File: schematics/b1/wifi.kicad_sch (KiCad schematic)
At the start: 14 parts, among them J1 SERIAL, SW2 RESET, SW3 BOOT, U2 ESP-12F, U9 MCP23017_SP

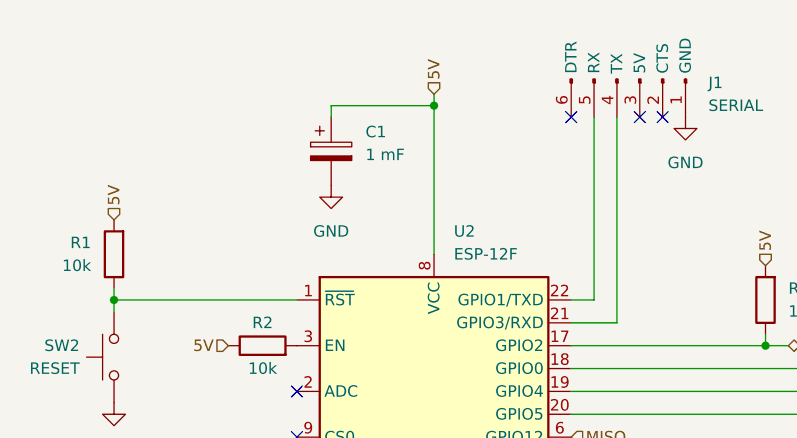
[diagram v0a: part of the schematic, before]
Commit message: Wired LoRa and added a bulk to the status block.
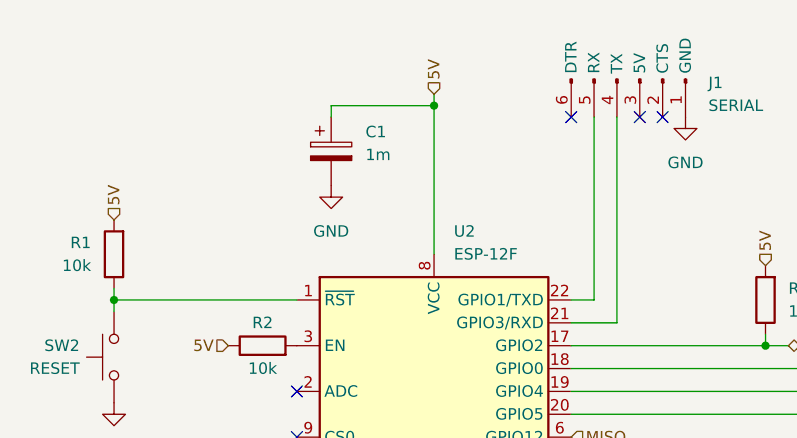
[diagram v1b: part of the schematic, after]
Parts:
- C1: value 1 mF -> 1m
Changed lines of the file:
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@@
       (effects (font (size 1.27 1.27)) (justify left))
     )
-    (property "Value" "1 mF" (at 85.09 62.611 0)
+    (property "Value" "1m" (at 85.09 62.611 0)
       (effects (font (size 1.27 1.27)) (justify left))
     )

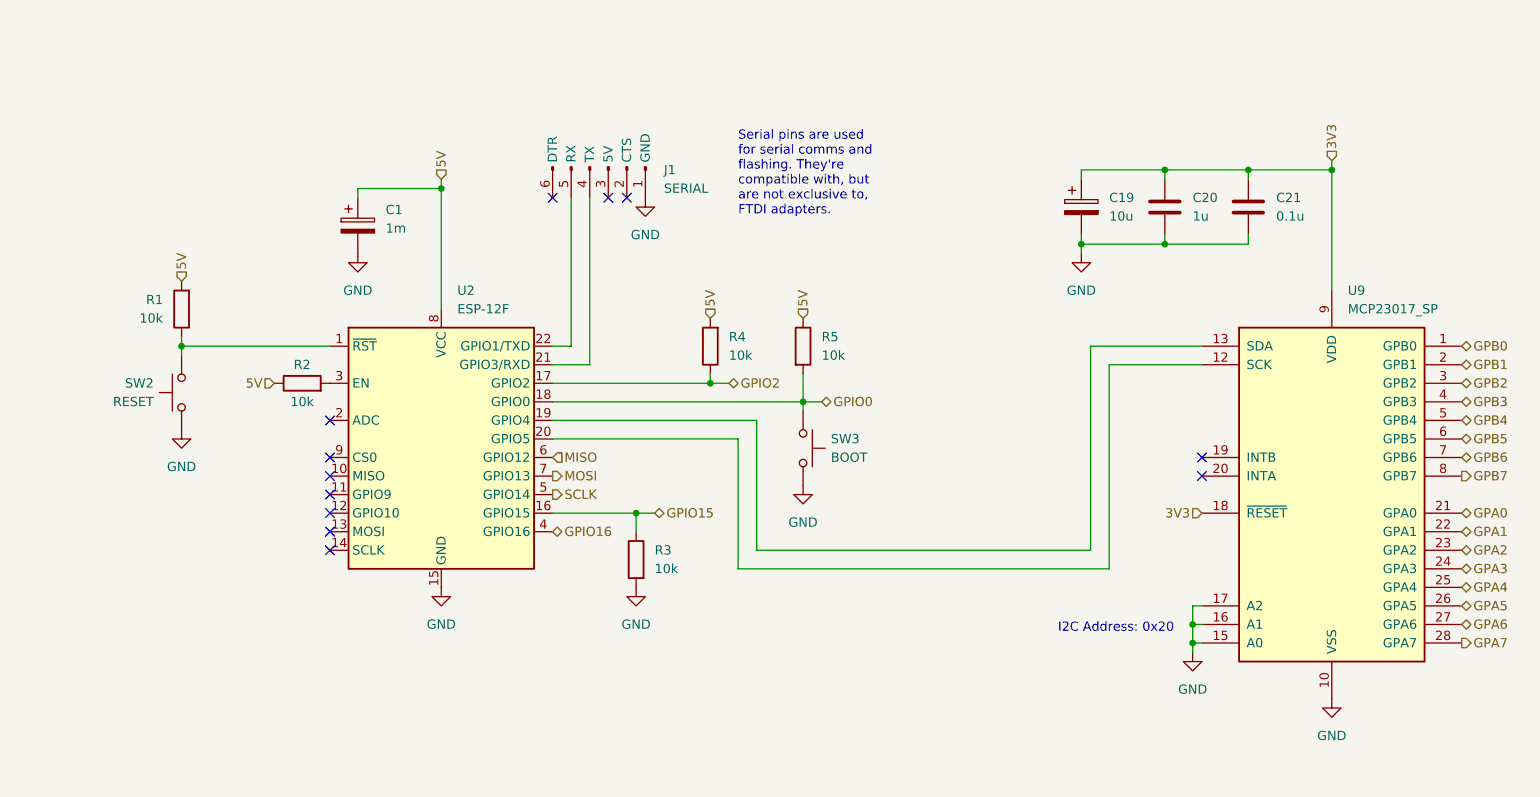
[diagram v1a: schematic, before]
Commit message: Increased capacitance and added some test points.
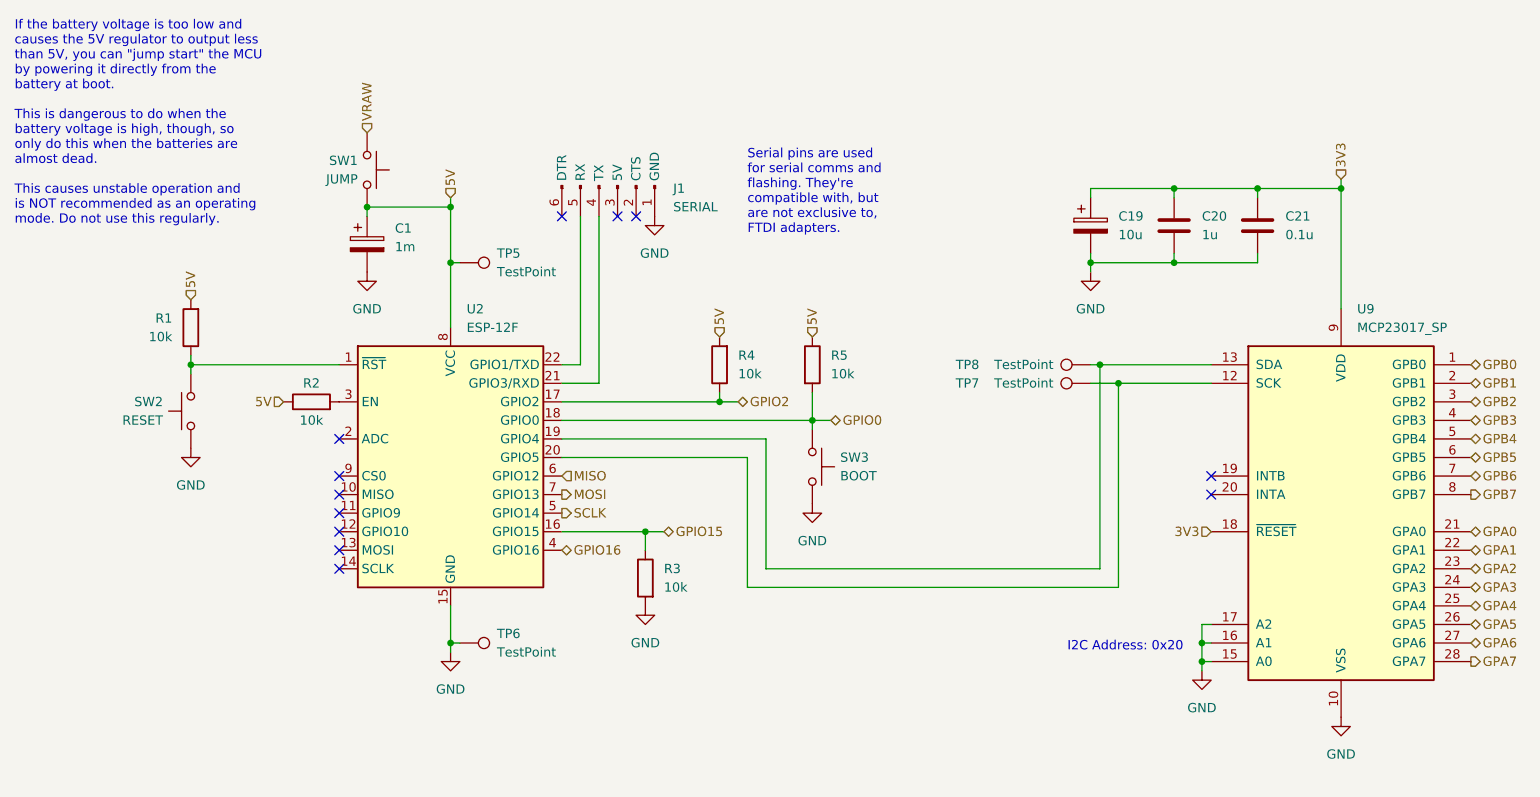
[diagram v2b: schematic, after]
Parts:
- added SW1: JUMP, symbol Switch:SW_Push
- added TP5, TP6, TP7, TP8: TestPoint, symbol Connector:TestPoint
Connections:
- net 5V: now also SW1.1, TP5.1
- net GND: now also TP6.1
- net at U2.19 (GPIO4), U9.13 (SDA): now also TP8.1
- net at U2.20 (GPIO5), U9.12 (SCK): now also TP7.1
- new net VRAW: SW1.2
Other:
- note added: "If the battery voltage is too low and causes the 5V regulator to output less than 5V, you can "jump start" the MCU by powering it directly from the battery at boot. This is dangerous to do when the battery voltage is high, though, so only do this when the batteries are almost dead. This causes unstable operation and is NOT recommended as an operating mode. Do not use this regularly."
- moved on the sheet: C1, C19, C20, C21, J1, R1, R2, R3, R4, R5, SW2, SW3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

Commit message: Added a bunch of test points.
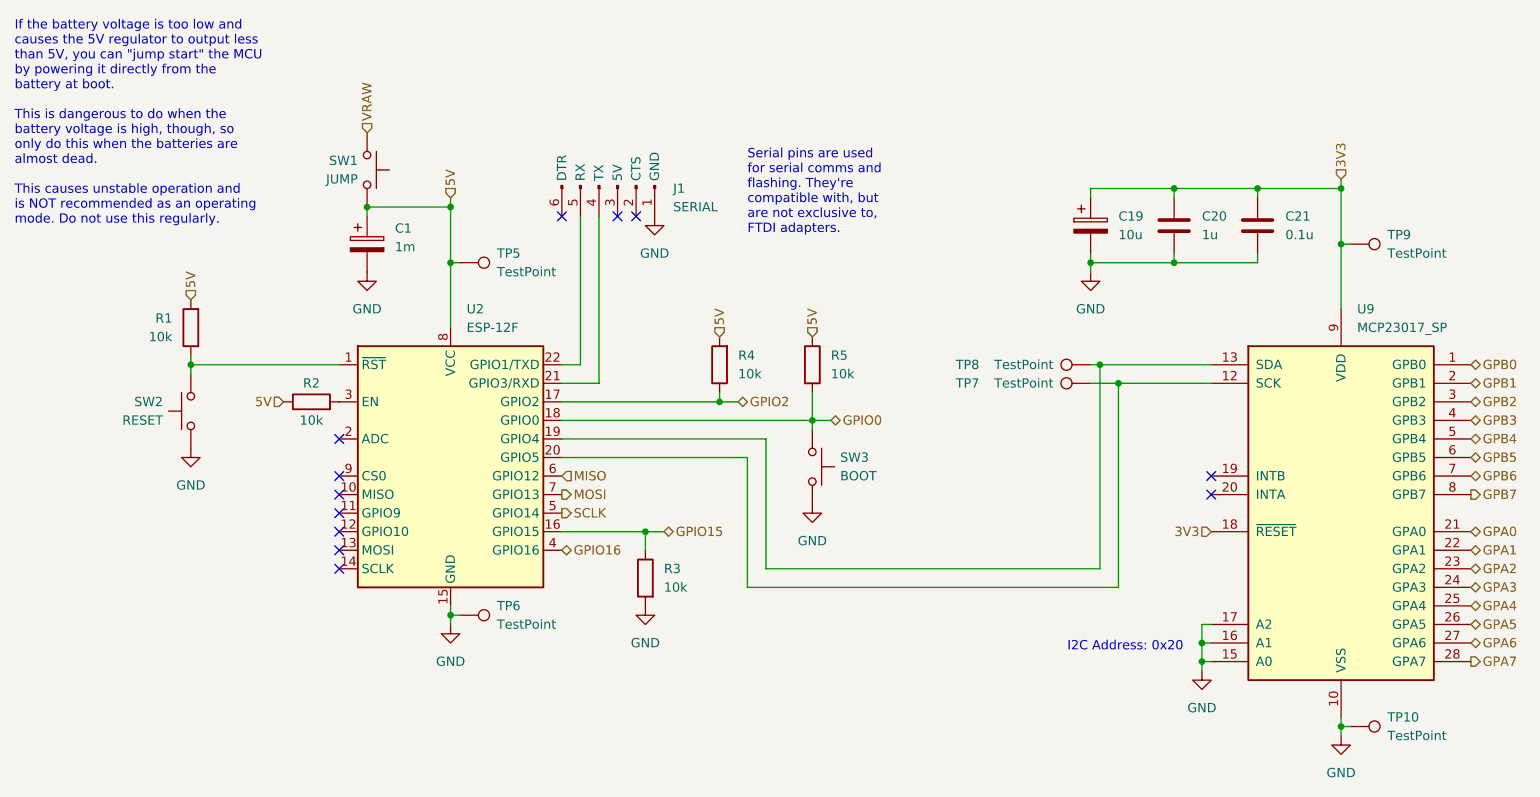
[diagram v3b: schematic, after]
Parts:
- added TP10, TP9: TestPoint, symbol Connector:TestPoint
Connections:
- net 3V3: now also TP9.1
- net GND: now also TP10.1
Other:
- moved on the sheet: TP6
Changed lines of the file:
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@@
   (junction (at 193.04 57.15) (diameter 0) (color 0 0 0 0)
   )
-  (junction (at 93.98 119.38) (diameter 0) (color 0 0 0 0)
+  (junction (at 93.98 115.57) (diameter 0) (color 0 0 0 0)
   )
   (junction (at 185.42 83.82) (diameter 0) (color 0 0 0 0)
@@
   (junction (at 82.55 59.69) (diameter 0) (color 0 0 0 0)
   )
+  (junction (at 215.9 64.77) (diameter 0) (color 0 0 0 0)
+  )
   (junction (at 215.9 57.15) (diameter 0) (color 0 0 0 0)
   )
@@
   )
   (junction (at 196.85 121.92) (diameter 0) (color 0 0 0 0)
+  )
+  (junction (at 215.9 130.81) (diameter 0) (color 0 0 0 0)
   )
   (junction (at 58.42 81.28) (diameter 0) (color 0 0 0 0)
@@
     (stroke (width 0) (type default))
   )
-  (wire (pts (xy 93.98 120.65) (xy 93.98 119.38))
+  (wire (pts (xy 93.98 116.84) (xy 93.98 115.57))
     (stroke (width 0) (type default))
   )
@@
     (stroke (width 0) (type default))
   )
+  (wire (pts (xy 215.9 132.08) (xy 215.9 130.81))
+    (stroke (width 0) (type default))
+  )
   (wire (pts (xy 181.61 68.58) (xy 181.61 67.31))
     (stroke (width 0) (type default))
@@
     (stroke (width 0) (type default))
   )
-  (wire (pts (xy 93.98 119.38) (xy 93.98 114.3))
+  (wire (pts (xy 93.98 115.57) (xy 93.98 114.3))
     (stroke (width 0) (type default))
   )
@@
     (stroke (width 0) (type default))
   )
-  (wire (pts (xy 95.25 119.38) (xy 93.98 119.38))
+  (wire (pts (xy 95.25 115.57) (xy 93.98 115.57))
     (stroke (width 0) (type default))
   )
@@
     (stroke (width 0) (type default))
   )
+  (wire (pts (xy 217.17 130.81) (xy 215.9 130.81))
+    (stroke (width 0) (type default))
+  )
   (wire (pts (xy 109.22 104.14) (xy 120.65 104.14))
     (stroke (width 0) (type default))
@@
     (stroke (width 0) (type default))
   )
-  (wire (pts (xy 215.9 57.15) (xy 215.9 73.66))
+  (wire (pts (xy 215.9 57.15) (xy 215.9 64.77))
     (stroke (width 0) (type default))
   )
@@
     (stroke (width 0) (type default))
   )
+  (wire (pts (xy 215.9 64.77) (xy 215.9 73.66))
+    (stroke (width 0) (type default))
+  )
   (wire (pts (xy 130.81 86.36) (xy 130.81 85.09))
     (stroke (width 0) (type default))
@@
   )
   (wire (pts (xy 109.22 86.36) (xy 130.81 86.36))
+    (stroke (width 0) (type default))
+  )
+  (wire (pts (xy 217.17 64.77) (xy 215.9 64.77))
+    (stroke (width 0) (type default))
+  )
+  (wire (pts (xy 215.9 130.81) (xy 215.9 129.54))
     (stroke (width 0) (type default))
   )
@@
     )
   )
-  (symbol (lib_id "Connector:TestPoint") (at 95.25 119.38 270) (unit 1)
+  (symbol (lib_id "Connector:TestPoint") (at 95.25 115.57 270) (unit 1)
     (in_bom yes) (on_board yes) (dnp no) (fields_autoplaced)
-    (property "Reference" "TP6" (at 100.33 118.11 90)
-      (effects (font (size 1.27 1.27)) (justify left))
-    )
-    (property "Value" "TestPoint" (at 100.33 120.65 90)
-      (effects (font (size 1.27 1.27)) (justify left))
-    )
-    (property "Footprint" "" (at 95.25 124.46 0)
-      (effects (font (size 1.27 1.27)) hide)
-    )
-    (property "Datasheet" "~" (at 95.25 124.46 0)
+    (property "Reference" "TP6" (at 100.33 114.3 90)
+      (effects (font (size 1.27 1.27)) (justify left))
+    )
+    (property "Value" "TestPoint" (at 100.33 116.84 90)
+      (effects (font (size 1.27 1.27)) (justify left))
+    )
+    (property "Footprint" "" (at 95.25 120.65 0)
+      (effects (font (size 1.27 1.27)) hide)
+    )
+    (property "Datasheet" "~" (at 95.25 120.65 0)
       (effects (font (size 1.27 1.27)) hide)
     )
@@
         (path "/d6142fa5-2354-4512-9919-37616259c364/a74f58bd-54a1-4bdf-85a5-bb477b4492d8"
           (reference "TP6") (unit 1)
+        )
+      )
+    )
+  )
+  (symbol (lib_id "Connector:TestPoint") (at 217.17 64.77 270) (unit 1)
+    (in_bom yes) (on_board yes) (dnp no) (fields_autoplaced)
+    (property "Reference" "TP9" (at 222.25 63.5 90)
+      (effects (font (size 1.27 1.27)) (justify left))
+    )
+    (property "Value" "TestPoint" (at 222.25 66.04 90)
+      (effects (font (size 1.27 1.27)) (justify left))
+    )
+    (property "Footprint" "" (at 217.17 69.85 0)
+      (effects (font (size 1.27 1.27)) hide)
+    )
+    (property "Datasheet" "~" (at 217.17 69.85 0)
+      (effects (font (size 1.27 1.27)) hide)
+    )
+    (pin "1")
+    (instances
+      (project "b1"
+        (path "/d6142fa5-2354-4512-9919-37616259c364/a74f58bd-54a1-4bdf-85a5-bb477b4492d8"
+          (reference "TP9") (unit 1)
         )
       )
@@
         (path "/d6142fa5-2354-4512-9919-37616259c364/a74f58bd-54a1-4bdf-85a5-bb477b4492d8"
           (reference "#PWR02") (unit 1)
-        )
-      )
-    )
-  )
-  (symbol (lib_id "power:GND") (at 215.9 129.54 0) (unit 1)
-    (in_bom yes) (on_board yes) (dnp no)
-    (property "Reference" "#PWR030" (at 215.9 135.89 0)
-      (effects (font (size 1.27 1.27)) hide)
-    )
-    (property "Value" "GND" (at 215.9 134.62 0)
-      (effects (font (size 1.27 1.27)))
-    )
-    (property "Footprint" "" (at 215.9 129.54 0)
-      (effects (font (size 1.27 1.27)) hide)
-    )
-    (property "Datasheet" "" (at 215.9 129.54 0)
-      (effects (font (size 1.27 1.27)) hide)
-    )
-    (pin "1")
-    (instances
-      (project "b1"
-        (path "/d6142fa5-2354-4512-9919-37616259c364/a74f58bd-54a1-4bdf-85a5-bb477b4492d8"
-          (reference "#PWR030") (unit 1)
         )
       )
@@
     )
   )
+  (symbol (lib_id "power:GND") (at 215.9 132.08 0) (unit 1)
+    (in_bom yes) (on_board yes) (dnp no)
+    (property "Reference" "#PWR037" (at 215.9 138.43 0)
+      (effects (font (size 1.27 1.27)) hide)
+    )
+    (property "Value" "GND" (at 215.9 137.16 0)
+      (effects (font (size 1.27 1.27)))
+    )
+    (property "Footprint" "" (at 215.9 132.08 0)
+      (effects (font (size 1.27 1.27)) hide)
+    )
+    (property "Datasheet" "" (at 215.9 132.08 0)
+      (effects (font (size 1.27 1.27)) hide)
+    )
+    (pin "1")
+    (instances
+      (project "b1"
+        (path "/d6142fa5-2354-4512-9919-37616259c364/a74f58bd-54a1-4bdf-85a5-bb477b4492d8"
+          (reference "#PWR037") (unit 1)
+        )
+      )
+    )
+  )
   (symbol (lib_id "power:GND") (at 143.51 100.33 0) (unit 1)
     (in_bom yes) (on_board yes) (dnp no) (fields_autoplaced)
@@
         (path "/d6142fa5-2354-4512-9919-37616259c364/a74f58bd-54a1-4bdf-85a5-bb477b4492d8"
           (reference "R4") (unit 1)
+        )
+      )
+    )
+  )
+  (symbol (lib_id "Connector:TestPoint") (at 217.17 130.81 270) (unit 1)
+    (in_bom yes) (on_board yes) (dnp no) (fields_autoplaced)
+    (property "Reference" "TP10" (at 222.25 129.54 90)
+      (effects (font (size 1.27 1.27)) (justify left))
+    )
+    (property "Value" "TestPoint" (at 222.25 132.08 90)
+      (effects (font (size 1.27 1.27)) (justify left))
+    )
+    (property "Footprint" "" (at 217.17 135.89 0)
+      (effects (font (size 1.27 1.27)) hide)
+    )
+    (property "Datasheet" "~" (at 217.17 135.89 0)
+      (effects (font (size 1.27 1.27)) hide)
+    )
+    (pin "1")
+    (instances
+      (project "b1"
+        (path "/d6142fa5-2354-4512-9919-37616259c364/a74f58bd-54a1-4bdf-85a5-bb477b4492d8"
+          (reference "TP10") (unit 1)
         )
       )
@@
     )
   )
-  (symbol (lib_id "power:GND") (at 93.98 120.65 0) (unit 1)
-    (in_bom yes) (on_board yes) (dnp no)
-    (property "Reference" "#PWR03" (at 93.98 127 0)
-      (effects (font (size 1.27 1.27)) hide)
-    )
-    (property "Value" "GND" (at 93.98 125.73 0)
+  (symbol (lib_id "power:GND") (at 93.98 116.84 0) (unit 1)
+    (in_bom yes) (on_board yes) (dnp no)
+    (property "Reference" "#PWR03" (at 93.98 123.19 0)
+      (effects (font (size 1.27 1.27)) hide)
+    )
+    (property "Value" "GND" (at 93.98 121.92 0)
       (effects (font (size 1.27 1.27)))
     )
-    (property "Footprint" "" (at 93.98 120.65 0)
-      (effects (font (size 1.27 1.27)) hide)
-    )
-    (property "Datasheet" "" (at 93.98 120.65 0)
-      (effects (font (size 1.27 1.27)) hide)
-    )
+    (property "Footprint" "" (at 93.98 116.84 0)
+      (effects (font (size 1.27 1.27)) hide)
+    )
+    (property "Datasheet" "" (at 93.98 116.84 0)
+      (effects (font (size 1.27 1.27)) hide)
+    )

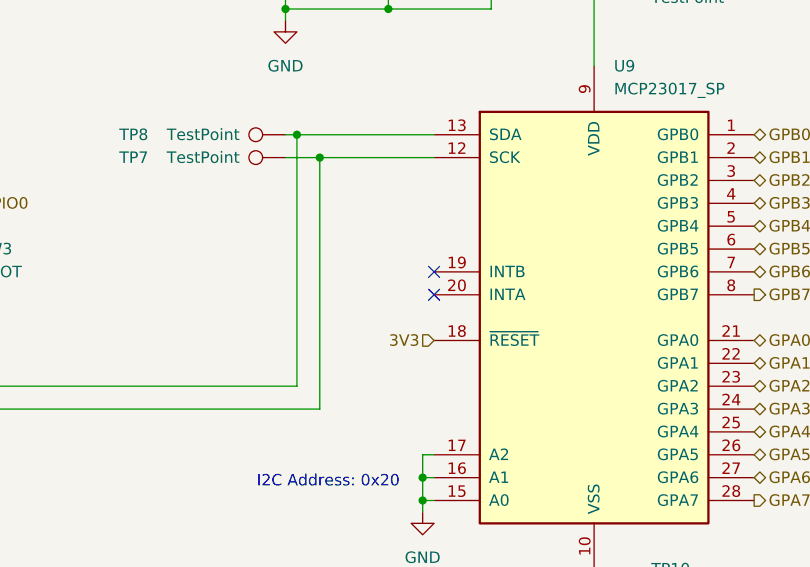
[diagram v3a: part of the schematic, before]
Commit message: Added optional interrupt pin to MCU for LoRa module.
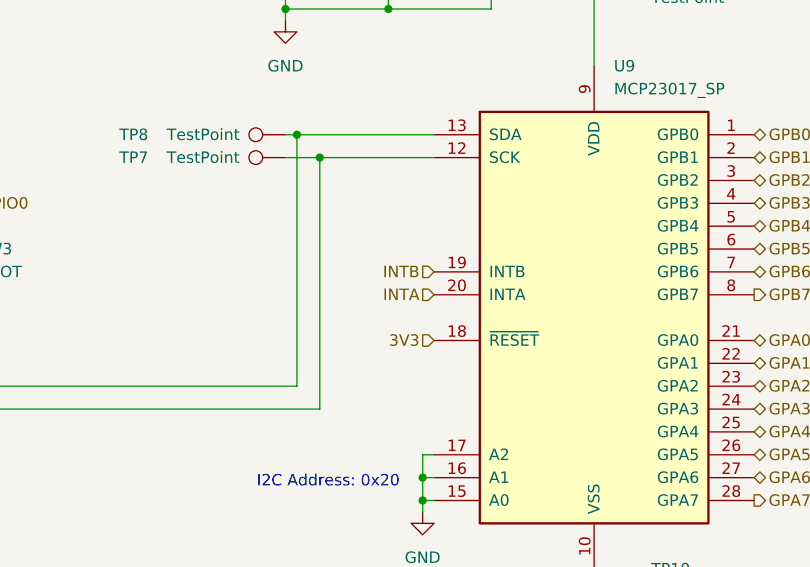
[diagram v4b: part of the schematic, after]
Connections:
- net INTB: now reaches U9.19 (INTB)
- net INTA: now reaches U9.20 (INTA)
- no-connect marks 12 -> 10
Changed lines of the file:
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@@
   )
   (no_connect (at 78.74 101.6))
-  (no_connect (at 198.12 99.06))
   (no_connect (at 78.74 96.52))
   (no_connect (at 78.74 106.68))
@@
   (no_connect (at 78.74 109.22))
   (no_connect (at 109.22 60.96))
-  (no_connect (at 198.12 96.52))
   (no_connect (at 78.74 104.14))
   (no_connect (at 116.84 60.96))
@@
     (effects (font (size 1.27 1.27)) (justify left))
   )
+  (hierarchical_label "INTB" (shape input) (at 198.12 96.52 180) (fields_autoplaced)
+    (effects (font (size 1.27 1.27)) (justify right))
+  )
+  (hierarchical_label "INTA" (shape input) (at 198.12 99.06 180) (fields_autoplaced)
+    (effects (font (size 1.27 1.27)) (justify right))
+  )
   (hierarchical_label "GPB0" (shape bidirectional) (at 233.68 81.28 0) (fields_autoplaced)

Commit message: Updated annotations.
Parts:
- renumbered C19 to C14, C20 to C15, C21 to C16, C1 to C17, R4 to R2, R5 to R3, R2 to R4, R3 to R5, SW1 to SW2, SW2 to SW3, SW3 to SW4, TP9 to TP20, TP5 to TP21, TP8 to TP22, TP7 to TP23, TP6 to TP24, TP10 to TP25, U2 to U3, U9 to U4

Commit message: Finalizing touches to the B1 schematic.
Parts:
- SW4: value BOOT -> FLASH
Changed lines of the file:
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@@
   (title_block
     (title "B1")
-    (date "2024-02-19")
+    (date "2024-02-20")
     (rev "1")
     (company "shawnd.xyz")
@@
       (effects (font (size 1.27 1.27)) (justify left))
     )
-    (property "Value" "BOOT" (at 147.32 96.52 90)
-      (effects (font (size 1.27 1.27)) (justify left))
-    )
+    (property "Value" "FLASH" (at 147.32 96.52 90)
+      (effects (font (size 1.27 1.27)) (justify left))
+    )
